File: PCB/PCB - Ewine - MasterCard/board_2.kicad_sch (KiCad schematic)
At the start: 37 parts, among them IC1 REG1117, U1 473460001, U3 STM32WB55RGV7

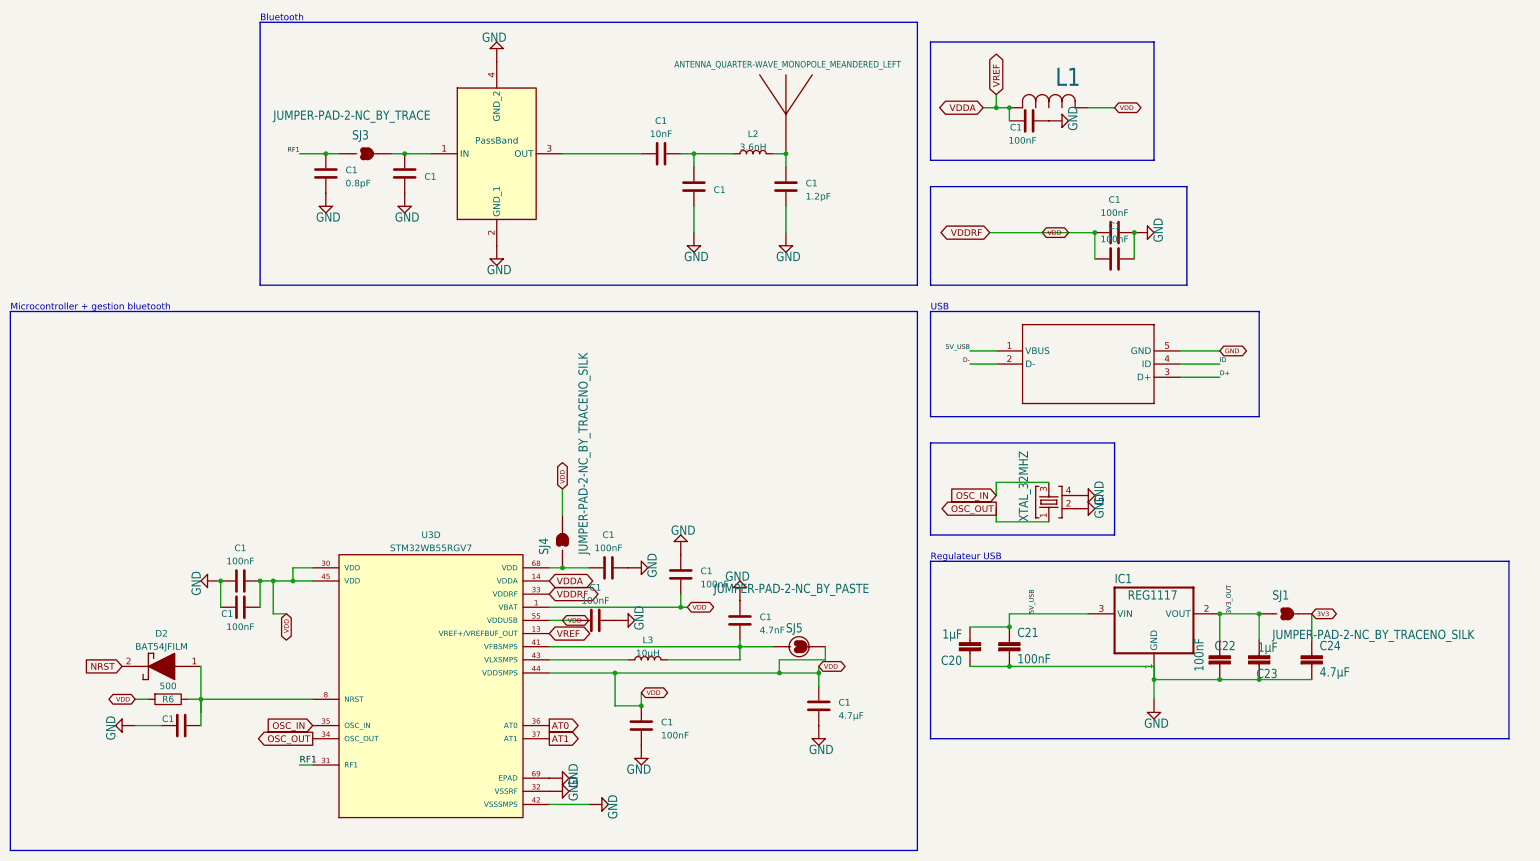
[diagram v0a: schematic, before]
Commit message: pcb master card ok + il reste à mettre les pins des capteurs restants
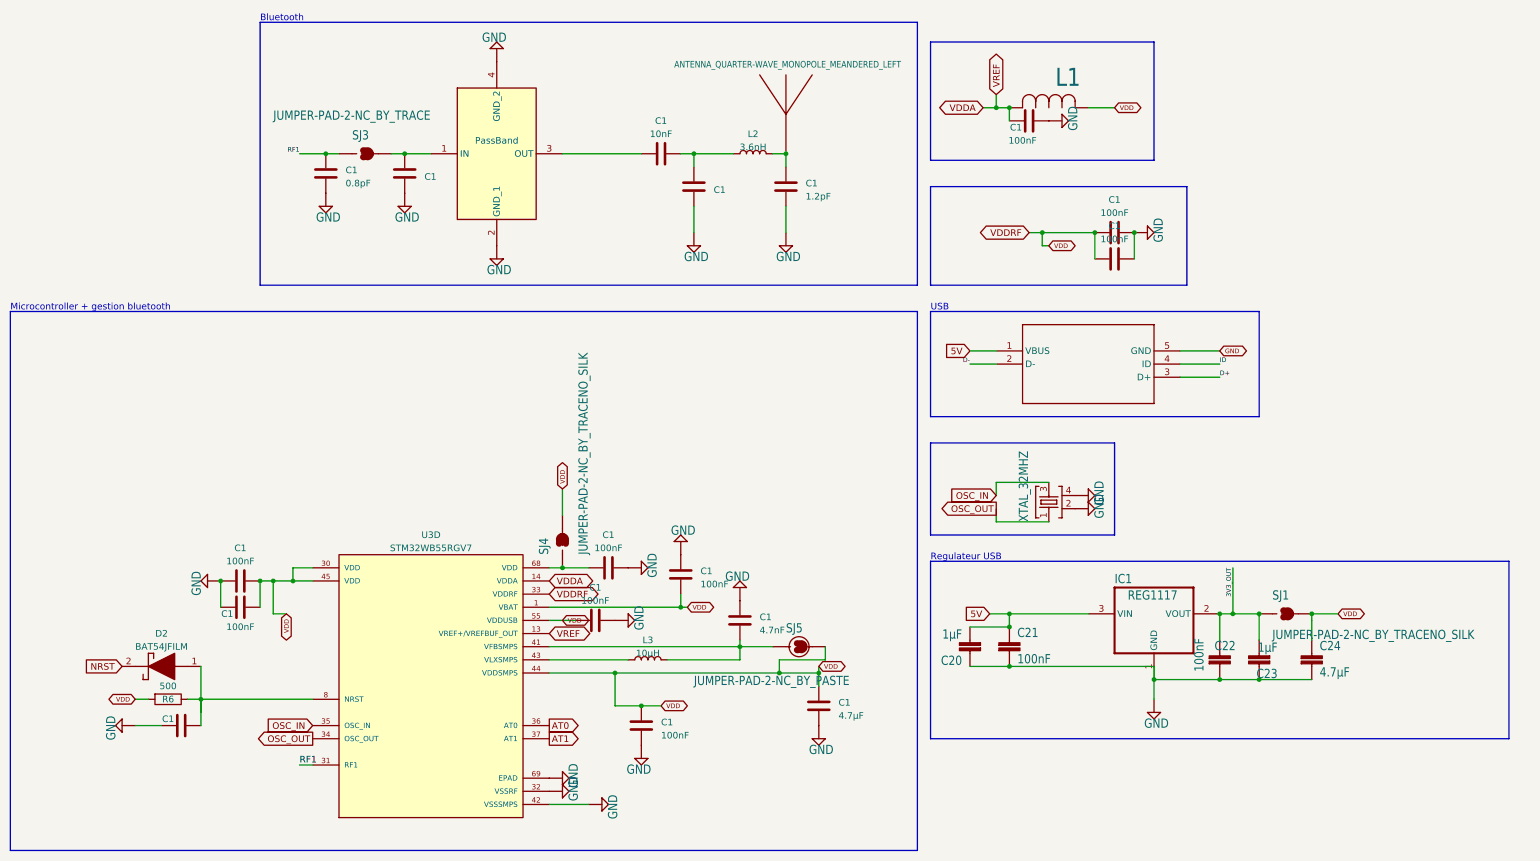
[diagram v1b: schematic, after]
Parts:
- C1: footprint Capacitor_SMD:C_0402_1005Metric -> Capacitor_SMD:C_0603_1608Metric
- C20, C23: footprint board:0805 -> Capacitor_SMD:C_0603_1608Metric
- C21, C22, C24: footprint board:0603-CAP -> Capacitor_SMD:C_0603_1608Metric
- D2: footprint SOD2513X117N -> Library:STM32WB55RG_Diode
- FL1: footprint FI212B245026T -> Library:STM32WB55RG_PassBand
- IC1: footprint board:SOT223 -> Package_TO_SOT_SMD:SOT-223
- L1: footprint board:IND_BLM15_0402_MUR -> Inductor_SMD:L_0603_1608Metric
- L2, L3: footprint Inductor_SMD:L_0402_1005Metric -> Inductor_SMD:L_0603_1608Metric
- R6: footprint Resistor_SMD:R_0402_1005Metric -> Resistor_SMD:R_0603_1608Metric
- SJ1, SJ4: footprint board:PAD-JUMPER-2-NC_BY_TRACE_NO_SILK -> Jumper:SolderJumper-2_P1.3mm_Bridged_RoundedPad1.0x1.5mm
- SJ3: footprint board:PAD-JUMPER-2-NC_BY_TRACE_YES_SILK -> Jumper:SolderJumper-2_P1.3mm_Bridged_RoundedPad1.0x1.5mm
- SJ5: footprint board:PAD-JUMPER-2-NC_BY_PASTE_YES_SILK -> Jumper:SolderJumper-2_P1.3mm_Bridged_RoundedPad1.0x1.5mm
- U$1: footprint board:BT-XTAL_2016_N -> Library:STM32WB55RG_XTAL
- U$6: footprint board:QWMP_MEANDERED_LEFT_+6 -> Library:STM32WB55RG_BleAntenna
- U1: footprint board:47346-0001_MOL -> Connector_USB:USB_Micro-B_Amphenol_10118194_Horizontal
- U3: footprint STM32WB55RGV7:QFN40P800X800X100-69N -> Library:STM32WB55RG
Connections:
- net 3V3 is gone; now on net VDD: C24.1, SJ1.2
- net 5V_USB renamed 5V
